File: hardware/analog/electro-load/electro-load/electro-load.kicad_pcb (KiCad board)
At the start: 2 copper layers, 76 parts, among them J1 Barrel_Jack, J3 AVR-ISP-10, K1 SANYOU_SRD_Form_C, M1 Noctua NF-A14 5V, Q1 Q_NJFET_GDS, Q2 2N2222A, Q3 2N2222, Q4 2N2222A, U2 ATmega328P-AU, U3 MCP4725A0T-E_CH, U4 LM358DR, U5 LM358DR, U6 NCP1406SNT1G

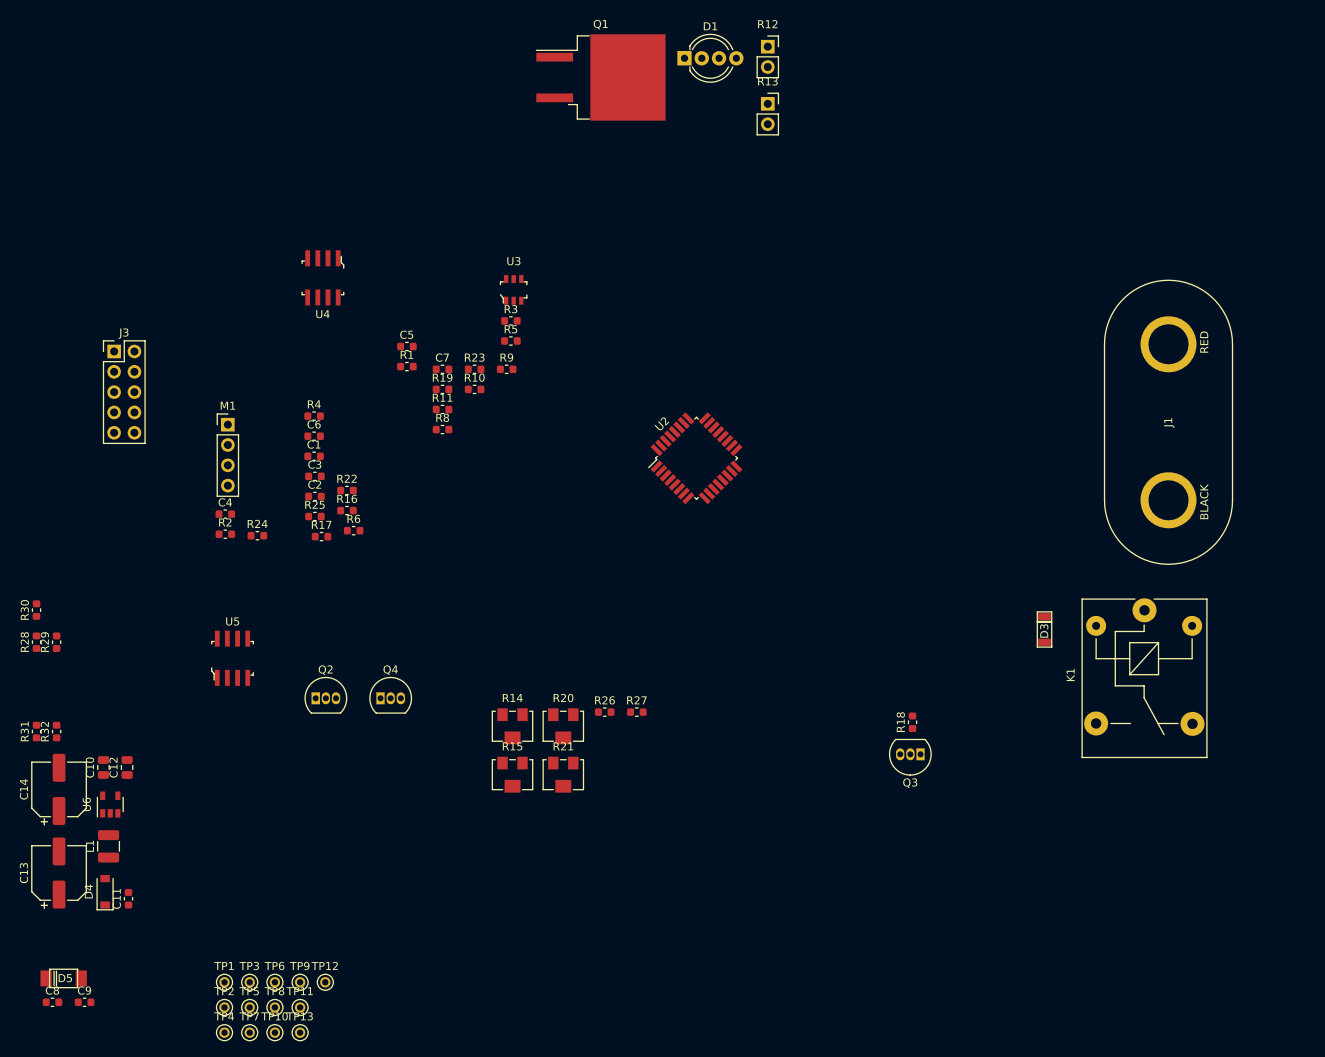
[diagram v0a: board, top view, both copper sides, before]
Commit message: Spread schematic out into multiple subsheets. Removed LEDs as pins was needed for 16x2 display
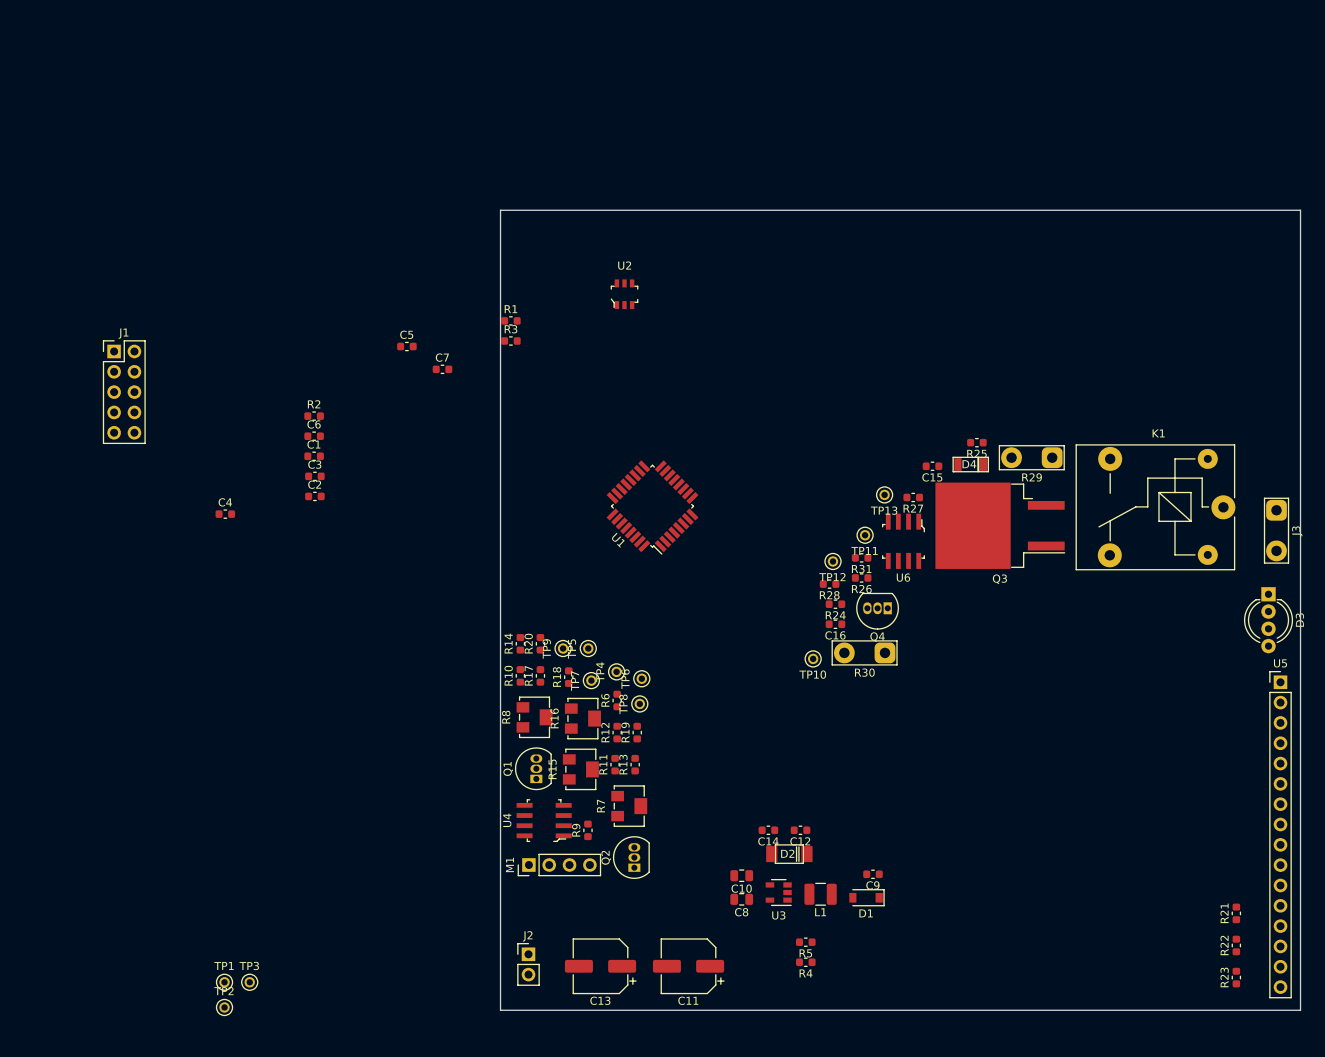
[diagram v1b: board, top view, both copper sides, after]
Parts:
- removed the D1 at (183.0, 46.0)
- removed the J1 at (243.5, 91.5)
- removed the R1 at (148.3, 84.5)
- removed the R2 at (125.6, 105.5)
- added C15: 100n 25V, Capacitor_SMD:C_0603_1608Metric, F.Cu at (214.0, 97.0)
- added C16: 100n 25V, Capacitor_SMD:C_0603_1608Metric, F.Cu at (201.9, 116.8)
- added D4: D_Schottky, athir:SOD80C(Reflow), F.Cu at (218.8, 96.8)
- added J2: Jack-DC, Connector_PinHeader_2.54mm:PinHeader_1x02_P2.54mm_Vertical, F.Cu at (163.5, 158.0)
- added J3: Barrel_Jack, TestPoint:TestPoint_2Pads_Pitch5.08mm_Drill1.3mm, F.Cu at (257.0, 102.5)
- added R31: 4k7, Resistor_SMD:R_0603_1608Metric, F.Cu at (205.1, 108.5)
- added R7: 10k POT, Potentiometer_SMD:Potentiometer_Bourns_3214W_Vertical, F.Cu at (176.1, 139.5)
- added U6: LM358DR, digikey-footprints:SOIC-8_W3.9mm, F.Cu at (210.4, 106.4)
- D3: value D_Schottky -> STATUS; footprint athir:SOD80C(Reflow) -> LED_THT:LED_D5.0mm-4_RGB_Wide_Pins
- Q1: value Q_NJFET_GDS -> 2N2222A; footprint Package_TO_SOT_SMD:TO-263-2 -> Package_TO_SOT_THT:TO-92_Inline
- Q3: value 2N2222 -> Q_NJFET_GDS; footprint Package_TO_SOT_THT:TO-92_Inline -> Package_TO_SOT_SMD:TO-263-2
- Q4: value 2N2222A -> 2N2222
- R10: value 2M -> 10k
- R11: value 825k -> 1k
- R12: value 2R 128++W -> 3k3; footprint Connector_PinSocket_2.54mm:PinSocket_1x02_P2.54mm_Vertical -> Resistor_SMD:R_0603_1608Metric
- R13: value 2ohm 128++W -> 1k; footprint Connector_PinSocket_2.54mm:PinSocket_1x02_P2.54mm_Vertical -> Resistor_SMD:R_0603_1608Metric
- R14: value 10k POT -> 1k; footprint Potentiometer_SMD:Potentiometer_Bourns_3214W_Vertical -> Resistor_SMD:R_0603_1608Metric
- R16: value 1k -> 10k POT; footprint Resistor_SMD:R_0603_1608Metric -> Potentiometer_SMD:Potentiometer_Bourns_3214W_Vertical
- R18: value 4k7 -> 10k
- R19: value 3k3 -> 1k
- R20: value 10k POT -> 3k3; footprint Potentiometer_SMD:Potentiometer_Bourns_3214W_Vertical -> Resistor_SMD:R_0603_1608Metric
- R21: value 10k POT -> 200; footprint Potentiometer_SMD:Potentiometer_Bourns_3214W_Vertical -> Resistor_SMD:R_0603_1608Metric
- R22: value 1k -> 2k
- R23: value 1k -> 220
- R25: value 3k3 -> 10M 1%
- R26: value 10k -> 1M5 1%
- R27: value 10k -> 2M
- R28: value 1k -> 825k
- R29: value 1k -> 2R 128++W; footprint Resistor_SMD:R_0603_1608Metric -> TestPoint:TestPoint_2Pads_Pitch5.08mm_Drill1.3mm
- R30: value 1k -> 2ohm 128++W; footprint Resistor_SMD:R_0603_1608Metric -> TestPoint:TestPoint_2Pads_Pitch5.08mm_Drill1.3mm
- R6: value 200 -> 1k
- R8: value 10M 1% -> 10k POT; footprint Resistor_SMD:R_0603_1608Metric -> Potentiometer_SMD:Potentiometer_Bourns_3214W_Vertical
- R9: value 1M5 1% -> 1k
- U5: value LM358DR -> RC1602A; footprint digikey-footprints:SOIC-8_W3.9mm -> Connector_PinHeader_2.54mm:PinHeader_1x16_P2.54mm_Vertical
- moved U5 131.0 mm to (257.5, 124.0)
- moved R29 126.6 mm to (229.0, 95.9), turned to 180 degrees
- moved R22 124.9 mm to (252.0, 156.9), turned to 90 degrees
- moved R23 121.8 mm to (252.0, 160.9), turned to 90 degrees
- moved R30 106.2 mm to (208.1, 120.3), turned to 180 degrees
- moved R4 100.4 mm to (198.2, 159.0), turned to 180 degrees
- moved R28 99.4 mm to (201.1, 111.7), turned to 180 degrees
- moved TP13 99.3 mm to (208.0, 100.6), turned to 180 degrees
- moved R5 97.3 mm to (198.2, 156.5), turned to 180 degrees
- moved C12 95.9 mm to (197.5, 142.5), turned to 180 degrees
- moved D1 95.1 mm to (205.7, 150.9), turned to 180 degrees
- moved C9 93.1 mm to (206.6, 148.0), turned to 180 degrees
- moved TP11 92.0 mm to (205.6, 105.6), turned to 180 degrees
- moved D2 92.0 mm to (196.1, 145.5), turned to 180 degrees
- moved L1 89.2 mm to (200.0, 150.5), turned to 180 degrees
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- renumbered C12 to C10, C13 to C11, C8 to C12, C14 to C13, C9 to C14, C10 to C8, C11 to C9, D4 to D1, D5 to D2, J3 to J1, R3 to R1, R4 to R2, R5 to R3, R31 to R4, R32 to R5, U2 to U1, U3 to U2, U6 to U3
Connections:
- D3 pad 1: +5V -> Net-(D3-Pad1)
- D3 pad 2: Net-(D3-Pad2) -> (no net)
- K1 pad 2: Net-(D3-Pad2) -> Net-(D4-Pad2)
- M1 pad 3: /FAN_RPM -> /Temperature Control/FAN_RPM
- M1 pad 4: /FAN_PWM -> /Temperature Control/FAN_PWM
- Q1 pad 1: Net-(Q1-Pad1) -> GND
- Q1 pad 2: Net-(K1-Pad3) -> Net-(Q1-Pad2)
- Q1 pad 3: Net-(Q1-Pad3) -> Net-(Q1-Pad2)
- Q3 pad 1: Net-(D3-Pad2) -> Net-(Q3-Pad1)
- Q3 pad 2: Net-(Q3-Pad2) -> Net-(K1-Pad3)
- Q3 pad 3: GND -> Net-(Q3-Pad3)
- Q4 pad 1: GND -> Net-(D4-Pad2)
- Q4 pad 3: Net-(Q4-Pad2) -> GND
- R10 pad 2: Net-(Q1-Pad3) -> Net-(R10-Pad2)
- R11 pad 1: GND -> Net-(R10-Pad1)
- R11 pad 2: Net-(R10-Pad1) -> Net-(R11-Pad2)
- R12 pad 1: GND -> +5V
- R12 pad 2: Net-(Q1-Pad3) -> Net-(Q1-Pad2)
- R13 pad 1: GND -> +5V
- R13 pad 2: Net-(Q1-Pad3) -> /Temperature Control/FAN_RPM
- R14 pad 1: Net-(R14-Pad1) -> (no net)
- R15 pad 2: +5V -> Net-(R14-Pad2)
- R16 pad 1: GND -> Net-(R16-Pad1)
- R16 pad 2: Net-(R15-Pad1) -> +5V
- R17 pad 1: Net-(R15-Pad1) -> GND
- R17 pad 2: Net-(R17-Pad2) -> Net-(R16-Pad1)
- R18 pad 1: Net-(Q3-Pad2) -> Net-(R16-Pad1)
- R18 pad 2: /RELAY_EN -> Net-(R15-Pad1)
- R19 pad 1: +5V -> Net-(R16-Pad1)
- R19 pad 2: Net-(Q2-Pad2) -> Net-(R19-Pad2)
- R20 pad 1: Net-(R20-Pad1) -> +5V
- R20 pad 2: Net-(R20-Pad2) -> Net-(Q2-Pad2)
- R21 pad 1: Net-(R21-Pad1) -> +5V
- R21 pad 2: +5V -> Net-(D3-Pad1)
- R22 pad 2: Net-(R21-Pad1) -> Net-(R22-Pad2)
- R23 pad 1: Net-(R21-Pad1) -> +5V
- R24 pad 1: +5V -> (no net)
- R24 pad 2: /FAN_RPM -> Net-(R24-Pad2)
- R25 pad 1: +5V -> /Current Measurements/V_IN
- R25 pad 2: Net-(Q4-Pad2) -> Net-(K1-Pad3)
- R26 pad 1: Net-(R15-Pad1) -> GND
- R26 pad 2: Net-(R14-Pad1) -> /Current Measurements/V_IN
- R27 pad 1: Net-(R21-Pad1) -> Net-(R27-Pad1)
- R27 pad 2: Net-(R20-Pad1) -> Net-(Q3-Pad3)
- R28 pad 1: /CUR_MEAS -> GND
- R28 pad 2: Net-(R28-Pad2) -> Net-(R27-Pad1)
- R29 pad 1: /TEMP_0 -> GND
- R29 pad 2: Net-(R14-Pad2) -> Net-(Q3-Pad3)
- R30 pad 1: /TEMP_1 -> GND
- R30 pad 2: Net-(R20-Pad2) -> Net-(Q3-Pad3)
- R6 pad 1: +5V -> (no net)
- R6 pad 2: Net-(D1-Pad1) -> Net-(R6-Pad2)
- R8 pad 1: /V_IN -> Net-(R10-Pad1)
- R8 pad 2: Net-(K1-Pad3) -> +5V
- R9 pad 2: /V_IN -> Net-(R10-Pad1)
- TP10 pad 1: Net-(R20-Pad2) -> Net-(R24-Pad2)
- TP11 pad 1: /FAN_PWM -> /Current Measurements/V_IN
- TP12 pad 1: /FAN_RPM -> /Current Measurements/CUR_SET
- TP13 pad 1: Net-(R21-Pad1) -> /Current Measurements/RELAY_EN
- TP4 pad 1: Net-(R28-Pad2) -> Net-(R6-Pad2)
- TP5 pad 1: /V_IN -> Net-(R10-Pad1)
- TP6 pad 1: /CUR_SET -> /Temperature Control/FAN_PWM
- TP7 pad 1: Net-(R14-Pad2) -> /Temperature Control/FAN_RPM
- TP8 pad 1: Net-(R15-Pad1) -> Net-(R14-Pad2)
- TP9 pad 1: /RELAY_EN -> Net-(R16-Pad1)
- U1 pad 12: /FAN_RPM -> (no net)
- U1 pad 13: /FAN_PWM -> (no net)
- U1 pad 14: /RELAY_EN -> (no net)
- U1 pad 23: /CUR_MEAS -> (no net)
- U1 pad 25: /TEMP_1 -> (no net)
- U1 pad 26: /TEMP_0 -> (no net)
- U1 pad 30: /STATUS_B -> (no net)
- U1 pad 7: /STATUS_R -> (no net)
- U1 pad 8: /STATUS_G -> (no net)
- U2 pad 1: /CUR_SET -> (no net)
- U4 pad 1: Net-(Q1-Pad1) -> Net-(R6-Pad2)
- U4 pad 2: /CUR_SET -> Net-(R11-Pad2)
- U4 pad 3: Net-(R10-Pad1) -> Net-(Q1-Pad2)
- U4 pad 5: Net-(R10-Pad1) -> Net-(Q2-Pad2)
- U4 pad 6: Net-(R28-Pad2) -> Net-(R19-Pad2)
- U4 pad 7: Net-(R28-Pad2) -> Net-(R14-Pad2)
- U4 pad 8: VCC -> +5V
- U5 pad 1: Net-(R14-Pad2) -> GND
- U5 pad 2: Net-(R17-Pad2) -> +5V
- U5 pad 3: Net-(Q2-Pad2) -> Net-(R22-Pad2)
- U5 pad 4: GND -> (no net)
- U5 pad 5: Net-(Q4-Pad2) -> (no net)
- U5 pad 6: Net-(R23-Pad2) -> (no net)
- U5 pad 7: Net-(R20-Pad2) -> (no net)
- U5 pad 8: +5V -> (no net)
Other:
- board outline added: 100 x 100 mm

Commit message: HW rev 1 of electronic load PCB.
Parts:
- removed C16: 100n 25V, Capacitor_SMD:C_0603_1608Metric
- removed C8: 10u 5V, Capacitor_SMD:C_0805_2012Metric
- removed C9: 82p 25V, Capacitor_SMD:C_0603_1608Metric
- removed D1: MBR0530, Diode_SMD:D_SOD-123
- removed D2: PMEG4050EP,115, athir:SOD128
- removed D3: STATUS, LED_THT:LED_D5.0mm-4_RGB_Wide_Pins
- removed D4: D_Schottky, athir:SOD80C(Reflow)
- removed L1: 10u CBC3225T100KR, Inductor_SMD:L_1210_3225Metric
- removed Q3: Q_NJFET_GDS, Package_TO_SOT_SMD:TO-263-2
- removed R15: 10k POT, Potentiometer_SMD:Potentiometer_Bourns_3214W_Vertical
- added C18: 100n, Capacitor_SMD:C_0603_1608Metric, F.Cu at (125.5, 49.0)
- added C19: 100n, Capacitor_SMD:C_0603_1608Metric, F.Cu at (128.0, 49.0)
- added C20: 100n, Capacitor_SMD:C_0603_1608Metric, F.Cu at (137.8, 49.0)
- added D6: flyback, Diode_THT:D_DO-35_SOD27_P7.62mm_Horizontal, F.Cu at (107.0, 58.0)
- added D7: 5+V protection, Diode_THT:D_DO-35_SOD27_P7.62mm_Horizontal, F.Cu at (54.2, 51.0)
- added HS1: RS_176-4176, athir:Heatsink_Fischer_SK104-STC-STIC_35x13mm_2xDrill2.5mm, F.Cu at (65.5, 39.5)
- added Q5: 2N2222, Package_TO_SOT_THT:TO-92_Inline, F.Cu at (105.8, 46.0)
- added R32: 1k, Resistor_SMD:R_0603_1608Metric, F.Cu at (63.2, 73.0)
- added R33: 10k, Resistor_SMD:R_0603_1608Metric, F.Cu at (133.0, 49.0)
- added R34: 10k, Resistor_SMD:R_0603_1608Metric, F.Cu at (130.5, 49.0)
- added R35: 10k, Resistor_SMD:R_0603_1608Metric, F.Cu at (135.5, 49.0)
- added REF**: MountingHole_2.7mm_M2.5_ISO14580_Pad, MountingHole:MountingHole_2.7mm_M2.5_ISO14580_Pad, F.Cu at (91.8, 98.5)
- added REF**: MountingHole_2.7mm_M2.5_ISO14580_Pad, MountingHole:MountingHole_2.7mm_M2.5_ISO14580_Pad, F.Cu at (109.0, 35.5)
- added REF**: MountingHole_2.7mm_M2.5_ISO14580_Pad, MountingHole:MountingHole_2.7mm_M2.5_ISO14580_Pad, F.Cu at (53.5, 98.5)
- added RV1: 10k POT, Potentiometer_THT:Potentiometer_Bourns_3296W_Vertical, F.Cu at (89.0, 63.8)
- added RV2: 10k POT, Potentiometer_THT:Potentiometer_Bourns_3296W_Vertical, F.Cu at (89.0, 70.5)
- added RV3: 10k POT, Potentiometer_THT:Potentiometer_Bourns_3296W_Vertical, F.Cu at (82.0, 77.8)
- added RV4: 10k POT, Potentiometer_THT:Potentiometer_Bourns_3296W_Vertical, F.Cu at (74.5, 82.8)
- added RV5: 6k8 POT, Potentiometer_THT:Potentiometer_Bourns_3296W_Vertical, F.Cu at (45.5, 95.0)
- added RV6: 2k POT, Potentiometer_THT:Potentiometer_Bourns_3296W_Vertical, F.Cu at (45.5, 84.0)
- added RV7: 10k POT, Potentiometer_THT:Potentiometer_Bourns_3296W_Vertical, F.Cu at (45.5, 57.2)
- added RV8: 6k8 POT, Potentiometer_THT:Potentiometer_Bourns_3296W_Vertical, F.Cu at (45.5, 68.0)
- added SW2: Rotary_Encoder_Switch, Rotary_Encoder:RotaryEncoder_Alps_EC11E-Switch_Vertical_H20mm, F.Cu at (122.8, 35.5)
- C10: value 3u3 25V -> 100n; footprint Capacitor_SMD:C_0805_2012Metric -> Capacitor_SMD:C_0603_1608Metric
- C11, C13: value 100u -> 100n; footprint Capacitor_SMD:CP_Elec_6.3x7.7 -> Capacitor_SMD:C_0603_1608Metric
- C12: value 100n 5V -> 100n
- C14: value 100n 5V -> 1n
- C15: value 100n 25V -> 100n
- J2: value Jack-DC -> Conn_WallSocket_Earth; footprint Connector_PinHeader_2.54mm:PinHeader_1x02_P2.54mm_Vertical -> athir:230VAC_PLUG
- J3: value Barrel_Jack -> INPUT
- Q4: value 2N2222 -> IPP055N03L G; footprint Package_TO_SOT_THT:TO-92_Inline -> Package_TO_SOT_THT:TO-220-3_Vertical
- R10: value 10k -> 1k
- R12: value 3k3 -> 10k
- R16: value 10k POT -> 2k; footprint Potentiometer_SMD:Potentiometer_Bourns_3214W_Vertical -> Resistor_SMD:R_0603_1608Metric
- R17: value 1k -> 220
- R18: value 10k -> 1R 100W; footprint Resistor_SMD:R_0603_1608Metric -> TestPoint:TestPoint_2Pads_Pitch5.08mm_Drill1.3mm
- R20: value 3k3 -> 1R 100W; footprint Resistor_SMD:R_0603_1608Metric -> TestPoint:TestPoint_2Pads_Pitch5.08mm_Drill1.3mm
- R21: value 200 -> 1R 100W; footprint Resistor_SMD:R_0603_1608Metric -> TestPoint:TestPoint_2Pads_Pitch5.08mm_Drill1.3mm
- R22: value 2k -> 1k
- R23: value 220 -> 1R 100W; footprint Resistor_SMD:R_0603_1608Metric -> TestPoint:TestPoint_2Pads_Pitch5.08mm_Drill1.3mm
- R24: value 1k -> 10k
- R25: value 10M 1% -> 825R
- R26: value 1M5 1% -> 100
- R27: value 2M -> 1k
- R28: value 825k -> 1k5
- R29: value 2R 128++W -> 1k; footprint TestPoint:TestPoint_2Pads_Pitch5.08mm_Drill1.3mm -> Resistor_SMD:R_0603_1608Metric
- R30: value 2ohm 128++W -> 1k; footprint TestPoint:TestPoint_2Pads_Pitch5.08mm_Drill1.3mm -> Resistor_SMD:R_0603_1608Metric
- R31: value 4k7 -> 1k
- R4: value 2M2 -> 3k3 1%
- R5: value 110k -> 1k
- R7: value 10k POT -> 10k; footprint Potentiometer_SMD:Potentiometer_Bourns_3214W_Vertical -> Resistor_SMD:R_0603_1608Metric
- R8: value 10k POT -> 1k; footprint Potentiometer_SMD:Potentiometer_Bourns_3214W_Vertical -> Resistor_SMD:R_0603_1608Metric
- R9: value 1k -> 3k3 1%
- U3: value NCP1406SNT1G -> LMV321
- U4: value LM358DR -> LMV321; footprint digikey-footprints:SOIC-8_W3.9mm -> Package_TO_SOT_SMD:SOT-23-5
- U6: value LM358DR -> LMV324; footprint digikey-footprints:SOIC-8_W3.9mm -> Package_SO:SOIC-14_3.9x8.7mm_P1.27mm
- moved R23 200.0 mm to (61.8, 99.2)
- moved J3 178.1 mm to (92.5, 34.2), turned to 0 degrees
- moved R21 177.5 mm to (82.8, 99.2)
- moved R22 177.1 mm to (110.2, 50.8), turned to 270 degrees
- moved R29 171.3 mm to (59.5, 70.8)
- moved R25 168.9 mm to (52.0, 73.0)
- moved U5 168.0 mm to (100.5, 64.2), turned to 90 degrees
- moved C15 167.3 mm to (50.7, 60.5)
- moved R30 163.7 mm to (52.0, 70.8)
- moved Q4 161.9 mm to (62.9, 43.9), turned to 0 degrees
- moved K1 161.6 mm to (95.0, 57.5), turned to 90 degrees
- moved U6 158.2 mm to (58.5, 62.0), turned to 315 degrees
- moved R27 158.1 mm to (56.0, 73.0), turned to 0 degrees
- moved R5 156.8 mm to (77.8, 56.0), turned to 270 degrees
- moved R26 156.6 mm to (60.5, 51.0), turned to 90 degrees
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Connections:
- C10 pad 1: VCC -> +5V
- C12 pad 1: GND -> +5V
- C12 pad 2: +5V -> GND
- C14 pad 1: GND -> Net-(C14-Pad1)
- C14 pad 2: +5V -> Net-(C14-Pad2)
- C15 pad 1: VCC -> +5V
- K1 pad 1: Net-(J3-Pad2) -> Net-(K1-Pad1)
- K1 pad 2: Net-(D4-Pad2) -> Net-(D6-Pad2)
- K1 pad 3: Net-(K1-Pad3) -> Net-(J3-Pad2)
- M1 pad 3: /Temperature Control/FAN_RPM -> /FAN_RPM
- M1 pad 4: /Temperature Control/FAN_PWM -> /FAN_PWM
- Q4 pad 1: Net-(D4-Pad2) -> Net-(Q3-Pad1)
- Q4 pad 2: Net-(Q4-Pad2) -> Net-(K1-Pad1)
- Q4 pad 3: GND -> Net-(Q3-Pad3)
- R10 pad 1: Net-(R10-Pad1) -> GND
- R11 pad 1: Net-(R10-Pad1) -> Net-(R11-Pad1)
- R11 pad 2: Net-(R11-Pad2) -> Net-(Q2-Pad2)
- R12 pad 1: +5V -> Net-(R12-Pad1)
- R12 pad 2: Net-(Q1-Pad2) -> Net-(R12-Pad2)
- R13 pad 1: +5V -> /TEMP_0
- R13 pad 2: /Temperature Control/FAN_RPM -> Net-(R12-Pad1)
- R14 pad 1: (no net) -> +5V
- R14 pad 2: Net-(R14-Pad2) -> /FAN_RPM
- R16 pad 1: Net-(R16-Pad1) -> GND
- R16 pad 2: +5V -> Net-(R16-Pad2)
- R17 pad 1: GND -> +5V
- R17 pad 2: Net-(R16-Pad1) -> Net-(R17-Pad2)
- R18 pad 1: Net-(R16-Pad1) -> Net-(Q3-Pad3)
- R18 pad 2: Net-(R15-Pad1) -> GND
- R19 pad 1: Net-(R16-Pad1) -> GND
- R20 pad 1: +5V -> Net-(Q3-Pad3)
- R20 pad 2: Net-(Q2-Pad2) -> GND
- R21 pad 1: +5V -> Net-(Q3-Pad3)
- R21 pad 2: Net-(D3-Pad1) -> GND
- R22 pad 1: GND -> Net-(Q5-Pad2)
- R22 pad 2: Net-(R22-Pad2) -> /RELAY_EN
- R23 pad 1: +5V -> Net-(Q3-Pad3)
- R23 pad 2: Net-(R23-Pad2) -> GND
- R24 pad 1: (no net) -> GND
- R24 pad 2: Net-(R24-Pad2) -> Net-(Q5-Pad2)
- R25 pad 1: /Current Measurements/V_IN -> GND
- R25 pad 2: Net-(K1-Pad3) -> Net-(R25-Pad2)
- R26 pad 1: GND -> Net-(C14-Pad2)
- R26 pad 2: /Current Measurements/V_IN -> Net-(Q3-Pad1)
- R27 pad 1: Net-(R27-Pad1) -> Net-(R25-Pad2)
- R27 pad 2: Net-(Q3-Pad3) -> Net-(C14-Pad1)
- R28 pad 1: GND -> Net-(D7-Pad1)
- R28 pad 2: Net-(R27-Pad1) -> GND
- R29 pad 1: GND -> Net-(Q3-Pad3)
- R29 pad 2: Net-(Q3-Pad3) -> Net-(R29-Pad2)
- R30 pad 2: Net-(Q3-Pad3) -> Net-(R30-Pad2)
- R31 pad 1: Net-(Q4-Pad2) -> Net-(R31-Pad1)
- R31 pad 2: /Current Measurements/RELAY_EN -> /V_MEAS
- R4 pad 1: VCC -> +5V
- R4 pad 2: Net-(C9-Pad2) -> Net-(Q1-Pad2)
- R5 pad 1: Net-(C9-Pad2) -> GND
- R5 pad 2: GND -> Net-(R5-Pad2)
- R6 pad 1: (no net) -> Net-(R6-Pad1)
- R6 pad 2: Net-(R6-Pad2) -> Net-(Q1-Pad2)
- R7 pad 1: Net-(R10-Pad2) -> Net-(R7-Pad1)
- R7 pad 2: Net-(R6-Pad2) -> Net-(R7-Pad2)
- R8 pad 1: Net-(R10-Pad1) -> /TEMP_1
- R8 pad 2: +5V -> Net-(R7-Pad1)
- R9 pad 1: GND -> +5V
- R9 pad 2: Net-(R10-Pad1) -> Net-(Q2-Pad2)
- TP10 pad 1: Net-(R24-Pad2) -> Net-(D7-Pad1)
- TP11 pad 1: /Current Measurements/V_IN -> Net-(C14-Pad2)
- TP12 pad 1: /Current Measurements/CUR_SET -> /V_MEAS
- TP13 pad 1: /Current Measurements/RELAY_EN -> /CUR_MEAS
- TP4 pad 1: Net-(R6-Pad2) -> /FAN_PWM
- TP5 pad 1: Net-(R10-Pad1) -> /FAN_RPM
- TP6 pad 1: /Temperature Control/FAN_PWM -> /CUR_SET
- TP7 pad 1: /Temperature Control/FAN_RPM -> Net-(J3-Pad2)
- TP8 pad 1: Net-(R14-Pad2) -> /RELAY_EN
- TP9 pad 1: Net-(R16-Pad1) -> Net-(TP9-Pad1)
- U1 pad 1: (no net) -> /LCD_RS
- U1 pad 10: (no net) -> /LCD_DB6
- U1 pad 11: (no net) -> /LCD_DB5
- U1 pad 12: (no net) -> /FAN_RPM
- U1 pad 13: (no net) -> /FAN_PWM
- U1 pad 14: (no net) -> /RELAY_EN
- U1 pad 2: (no net) -> /LCD_DB4
- U1 pad 23: (no net) -> /CUR_MEAS
- U1 pad 24: (no net) -> /V_MEAS
- U1 pad 25: (no net) -> /TEMP_1
- U1 pad 26: (no net) -> /TEMP_0
- U1 pad 30: (no net) -> /ROT_SW
- U1 pad 31: (no net) -> /LCD_EN
- U1 pad 32: (no net) -> /LCD_RW
- U1 pad 7: (no net) -> /ROT_A
- U1 pad 8: (no net) -> /ROT_B
- U1 pad 9: (no net) -> /LCD_DB7
- U2 pad 1: (no net) -> /CUR_SET
- U3 pad 1: (no net) -> Net-(R5-Pad2)
- U3 pad 2: Net-(C9-Pad2) -> GND
- U3 pad 3: +5V -> Net-(R6-Pad1)
- U3 pad 4: GND -> Net-(R7-Pad1)
- U3 pad 5: Net-(D1-Pad2) -> +5V
- U4 pad 1: Net-(R6-Pad2) -> Net-(R10-Pad2)
- U4 pad 2: Net-(R11-Pad2) -> GND
- U4 pad 3: Net-(Q1-Pad2) -> Net-(R11-Pad1)
- U4 pad 4: GND -> Net-(R12-Pad1)
- U4 pad 5: Net-(Q2-Pad2) -> +5V
- U5 pad 11: (no net) -> /LCD_DB4
- U5 pad 12: (no net) -> /LCD_DB5
- U5 pad 13: (no net) -> /LCD_DB6
- U5 pad 14: (no net) -> /LCD_DB7
- U5 pad 15: Net-(R23-Pad2) -> Net-(R17-Pad2)
- U5 pad 3: Net-(R22-Pad2) -> Net-(R16-Pad2)
- U5 pad 4: (no net) -> /LCD_RS
- U5 pad 5: (no net) -> /LCD_RW
- U5 pad 6: (no net) -> /LCD_EN
- U6 pad 1: Net-(Q3-Pad1) -> Net-(C14-Pad2)
- U6 pad 2: /Current Measurements/CUR_SET -> Net-(R25-Pad2)
- U6 pad 3: Net-(R27-Pad1) -> Net-(TP9-Pad1)
- U6 pad 4: GND -> +5V
- U6 pad 5: Net-(R27-Pad1) -> Net-(D7-Pad1)
- U6 pad 6: Net-(R24-Pad2) -> Net-(R31-Pad1)
- U6 pad 7: Net-(R24-Pad2) -> Net-(R31-Pad1)
- U6 pad 8: VCC -> Net-(R32-Pad1)
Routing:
- net +5V: track 0.00 -> 480.3 mm, vias 0 -> 25
- net Net-(Q3-Pad3): track 0.00 -> 167.2 mm, vias 0 -> 1
- net /CUR_MEAS: track 0.00 -> 78.7 mm, vias 0 -> 4
- net /V_MEAS: track 0.00 -> 76.3 mm, vias 0 -> 4
- net /SDA: track 0.00 -> 73.2 mm, vias 0 -> 4
- net /SCL: track 0.00 -> 70.8 mm, vias 0 -> 4
- net /ROT_A: track 0.00 -> 68.7 mm, vias 0 -> 6
- net Net-(K1-Pad1): track 0.00 -> 64.2 mm
- net /RELAY_EN: track 0.00 -> 61.2 mm, vias 0 -> 2
- net /ROT_B: track 0.00 -> 60.0 mm, vias 0 -> 8
- net Net-(R25-Pad2): track 0.00 -> 55.2 mm
- net /ROT_SW: track 0.00 -> 47.3 mm
- net Net-(R19-Pad2): track 0.00 -> 41.4 mm
- net /LCD_DB7: track 0.00 -> 39.9 mm
- net /TEMP_1: track 0.00 -> 39.4 mm, vias 0 -> 4
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- added copper zone on B.Cu, net GND
- added copper zone on F.Cu, net GND
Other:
- board size 100 x 100 mm -> 100 x 75 mm
- board text added: "Electro-Load 8A @ +30V Rev 1 2014"
